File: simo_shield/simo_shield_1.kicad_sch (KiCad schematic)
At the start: 10 parts, among them J1 modulo_usb_debug, J2 conector_bateria, U1 elemon_board, U2 modulo_flash_externa, U3 bluepill_board_stm32, U4 modulo_acelerometro

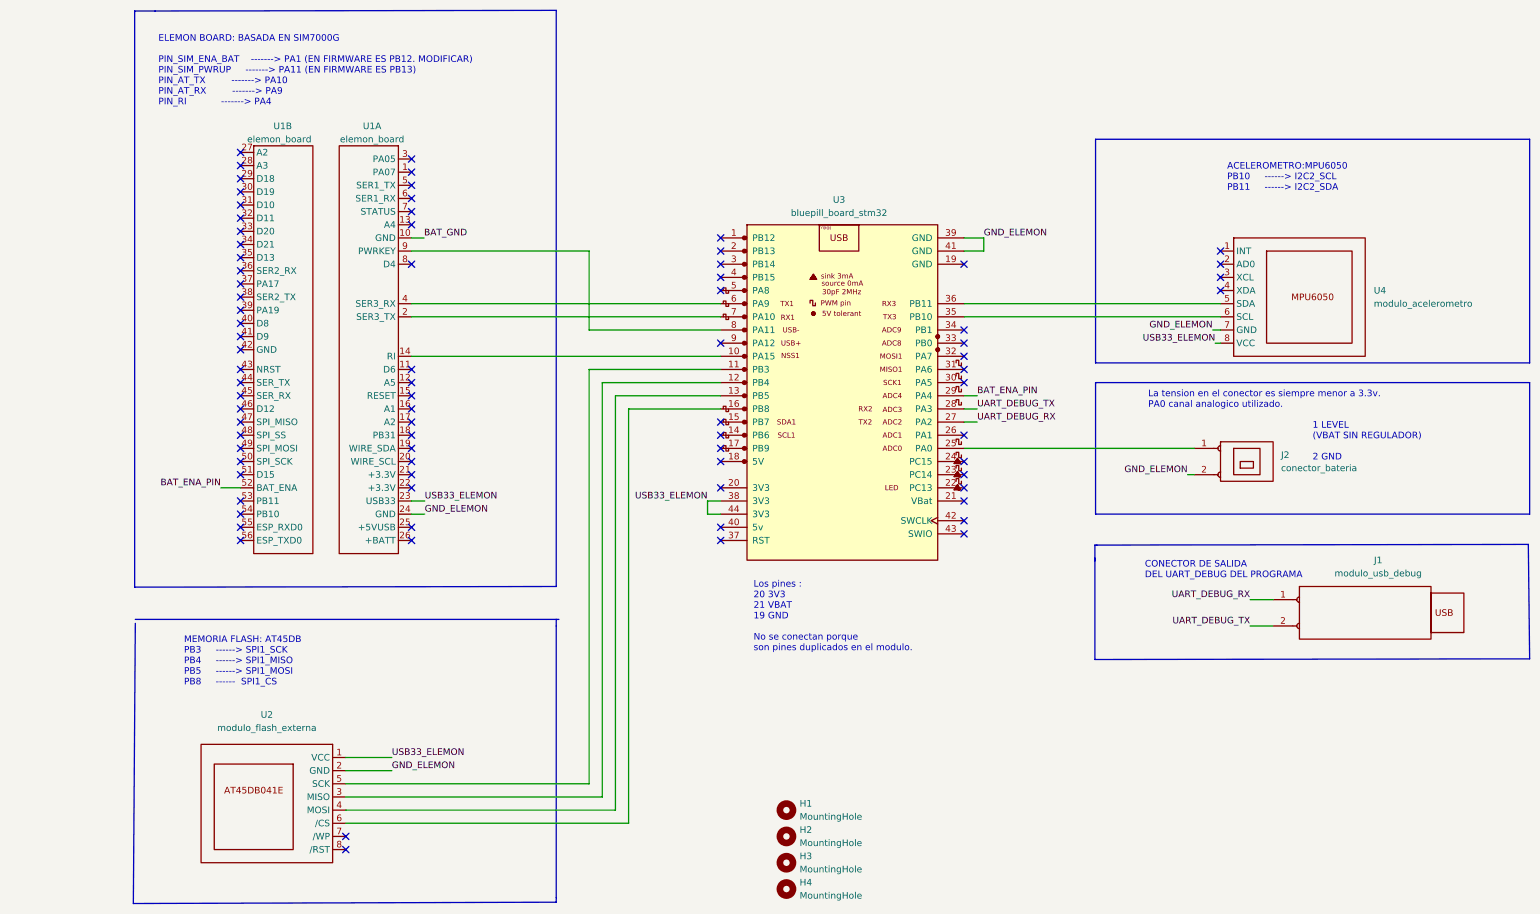
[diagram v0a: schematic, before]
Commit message: modificaciones simo shield: esquema y PCB. Detalle: se modifico la alimentacion y  eliminaron conectores custom
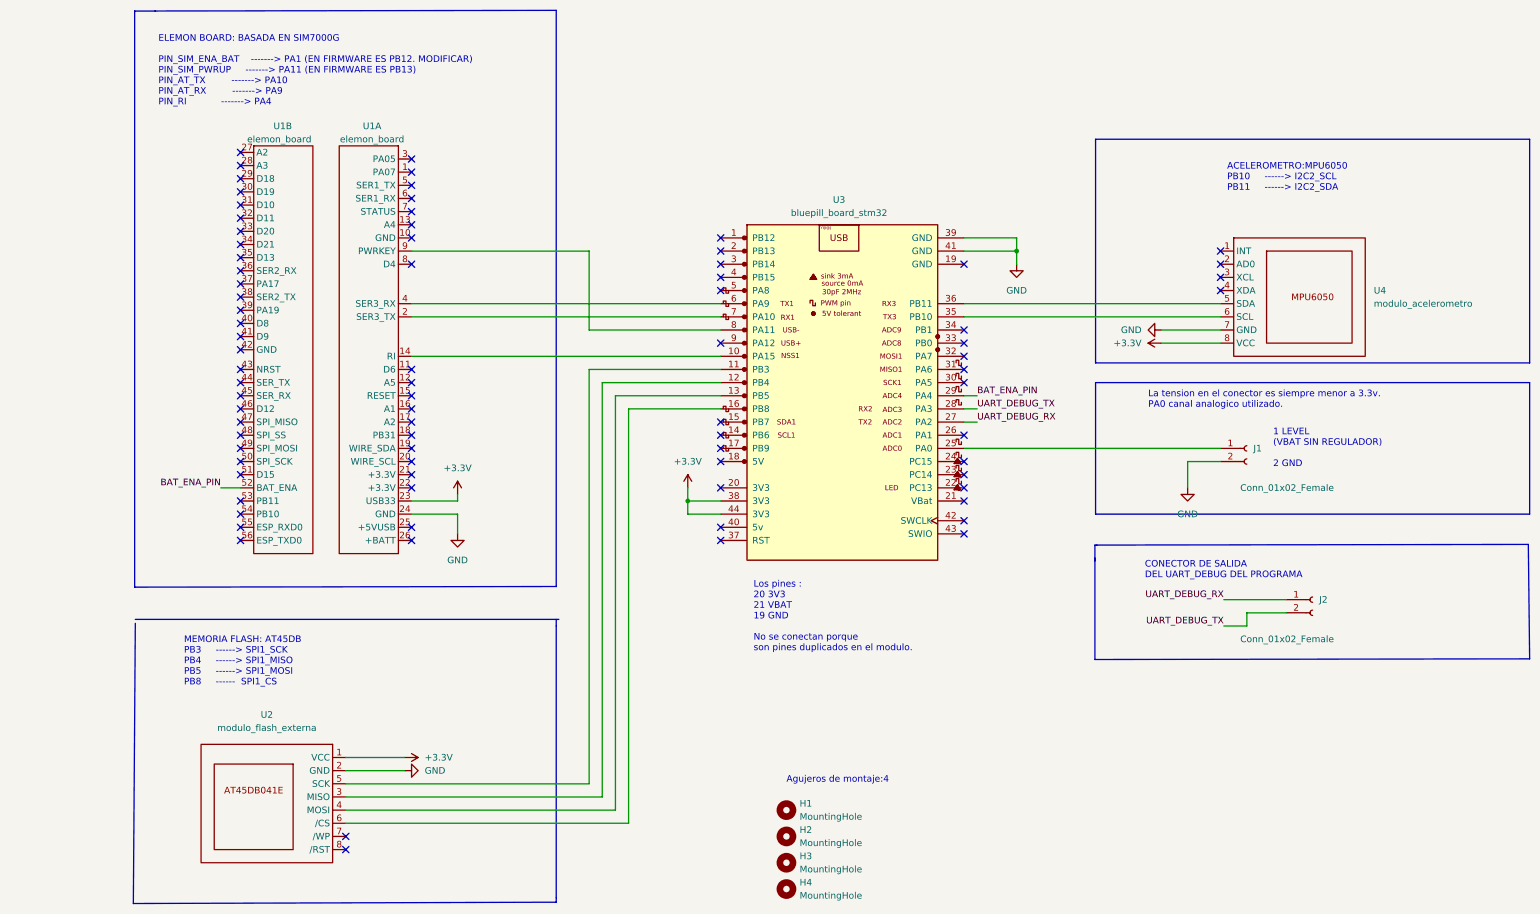
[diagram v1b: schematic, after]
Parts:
- removed J1: modulo_usb_debug, simo_shield:JST_EH_B2B-EH-A_1x02_P2.50mm_Vertical, symbol simo_shield:modulo_usb_debug
- removed J2: conector_bateria, simo_shield:JST_EH_B2B-EH-A_1x02_P2.50mm_Vertical, symbol simo_shield:conector_bateria
- added J1, J2: Conn_01x02_Female, simo_shield:JST_EH_B2B-EH-A_1x02_P2.50mm_Vertical, symbol simo_shield:Conn_01x02_Female
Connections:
- net UART_DEBUG_RX: now also J2.1 (Pin_1)
- net UART_DEBUG_TX: now also J2.2 (Pin_2)
- net at U3.25 (PA0): now also J1.1 (Pin_1)
- net BAT_GND: no longer names the net of U1.10 (GND)
- net GND_ELEMON renamed GND
- net GND: now also J1.2 (Pin_2)
- net USB33_ELEMON renamed +3.3V
- no-connect marks 80 -> 81
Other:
- note added: "Agujeros de montaje:4"

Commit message: actualizaciones a pcb y esquema simo shield
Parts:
- J1, J2: Codigo (none) -> B2B-EH-A(LF)(SN); Digikey (none) -> 455-1611-ND
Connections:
- net +3.3V: now also U4.7 (GND); no longer U4.8 (VCC)
- net GND: now also U4.8 (VCC); no longer U4.7 (GND)
- net at U1.9 (PWRKEY): now also U3.2 (PB13); no longer U3.8 (PA11)
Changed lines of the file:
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@@
   )
   (no_connect (at 127 118.11))
-  (no_connect (at 127 62.23))
+  (no_connect (at 127 77.47))
   (no_connect (at 127 69.85))
   (no_connect (at 127 80.01))
@@
     (stroke (width 0) (type default) (color 0 0 0 0))
   )
+  (wire (pts (xy 67.31 62.23) (xy 127 62.23))
+    (stroke (width 0) (type default) (color 0 0 0 0))
+  )
   (wire (pts (xy 212.09 80.01) (xy 223.52 80.01))
     (stroke (width 0) (type default) (color 0 0 0 0))
@@
     (stroke (width 0) (type default) (color 0 0 0 0))
   )
-  (wire (pts (xy 127 77.47) (xy 101.6 77.47))
-    (stroke (width 0) (type default) (color 0 0 0 0))
-  )
   (wire (pts (xy 120.65 110.49) (xy 127 110.49))
     (stroke (width 0) (type default) (color 0 0 0 0))
@@
     (stroke (width 0) (type default) (color 0 0 0 0))
   )
-  (wire (pts (xy 101.6 77.47) (xy 101.6 62.23))
-    (stroke (width 0) (type default) (color 0 0 0 0))
-  )
   (wire (pts (xy 106.68 90.17) (xy 127 90.17))
     (stroke (width 0) (type default) (color 0 0 0 0))
@@
   )
   (wire (pts (xy 224.155 134.62) (xy 228.6 134.62))
-    (stroke (width 0) (type default) (color 0 0 0 0))
-  )
-  (wire (pts (xy 67.31 62.23) (xy 101.6 62.23))
     (stroke (width 0) (type default) (color 0 0 0 0))
   )
@@
       (effects (font (size 1.27 1.27)) hide)
     )
-    (property "Datasheet" "~" (id 3) (at 228.6 100.33 0)
+    (property "Datasheet" "https://www.jst.fr/doc/jst/pdf/jst-connector-catalogue-vol-120e.pdf" (id 3) (at 228.6 100.33 0)
+      (effects (font (size 1.27 1.27)) hide)
+    )
+    (property "Digikey" "455-1611-ND" (id 4) (at 228.6 100.33 0)
+      (effects (font (size 1.27 1.27)) hide)
+    )
+    (property "Codigo" "B2B-EH-A(LF)(SN)" (id 5) (at 228.6 100.33 0)
       (effects (font (size 1.27 1.27)) hide)
     )
@@
       (effects (font (size 1.27 1.27)) hide)
     )
-    (property "Datasheet" "~" (id 3) (at 241.3 129.54 0)
+    (property "Datasheet" "https://www.jst.fr/doc/jst/pdf/jst-connector-catalogue-vol-120e.pdf" (id 3) (at 241.3 129.54 0)
+      (effects (font (size 1.27 1.27)) hide)
+    )
+    (property "Codigo" "B2B-EH-A(LF)(SN)" (id 4) (at 241.3 129.54 0)
+      (effects (font (size 1.27 1.27)) hide)
+    )
+    (property "Digikey" "455-1611-ND" (id 5) (at 241.3 129.54 0)
       (effects (font (size 1.27 1.27)) hide)
     )
@@
     (pin "2")
   )
-  (symbol (lib_id "simo_shield:+3.3V") (at 212.09 80.01 90) (unit 1)
-    (in_bom yes) (on_board yes) (fields_autoplaced)
-    (property "Reference" "#PWR0109" (id 0) (at 215.9 80.01 0)
-      (effects (font (size 1.27 1.27)) hide)
-    )
-    (property "Value" "+3.3V" (id 1) (at 208.28 80.0099 90)
-      (effects (font (size 1.27 1.27)) (justify left))
-    )
-    (property "Footprint" "" (id 2) (at 212.09 80.01 0)
-      (effects (font (size 1.27 1.27)) hide)
-    )
-    (property "Datasheet" "" (id 3) (at 212.09 80.01 0)
+  (symbol (lib_id "simo_shield:+3.3V") (at 212.09 77.47 90) (unit 1)
+    (in_bom yes) (on_board yes) (fields_autoplaced)
+    (property "Reference" "#PWR0109" (id 0) (at 215.9 77.47 0)
+      (effects (font (size 1.27 1.27)) hide)
+    )
+    (property "Value" "+3.3V" (id 1) (at 208.28 77.4699 90)
+      (effects (font (size 1.27 1.27)) (justify left))
+    )
+    (property "Footprint" "" (id 2) (at 212.09 77.47 0)
+      (effects (font (size 1.27 1.27)) hide)
+    )
+    (property "Datasheet" "" (id 3) (at 212.09 77.47 0)
       (effects (font (size 1.27 1.27)) hide)
     )
@@
     (pin "1")
   )
-  (symbol (lib_id "power:GND") (at 212.09 77.47 270) (unit 1)
-    (in_bom yes) (on_board yes) (fields_autoplaced)
-    (property "Reference" "#PWR0110" (id 0) (at 205.74 77.47 0)
-      (effects (font (size 1.27 1.27)) hide)
-    )
-    (property "Value" "GND" (id 1) (at 208.28 77.4699 90)
+  (symbol (lib_id "power:GND") (at 212.09 80.01 270) (unit 1)
+    (in_bom yes) (on_board yes) (fields_autoplaced)
+    (property "Reference" "#PWR0110" (id 0) (at 205.74 80.01 0)
+      (effects (font (size 1.27 1.27)) hide)
+    )
+    (property "Value" "GND" (id 1) (at 208.28 80.0099 90)
       (effects (font (size 1.27 1.27)) (justify right))
     )
-    (property "Footprint" "" (id 2) (at 212.09 77.47 0)
-      (effects (font (size 1.27 1.27)) hide)
-    )
-    (property "Datasheet" "" (id 3) (at 212.09 77.47 0)
-      (effects (font (size 1.27 1.27)) hide)
-    )
+    (property "Footprint" "" (id 2) (at 212.09 80.01 0)
+      (effects (font (size 1.27 1.27)) hide)
+    )
+    (property "Datasheet" "" (id 3) (at 212.09 80.01 0)
+      (effects (font (size 1.27 1.27)) hide)
+    )

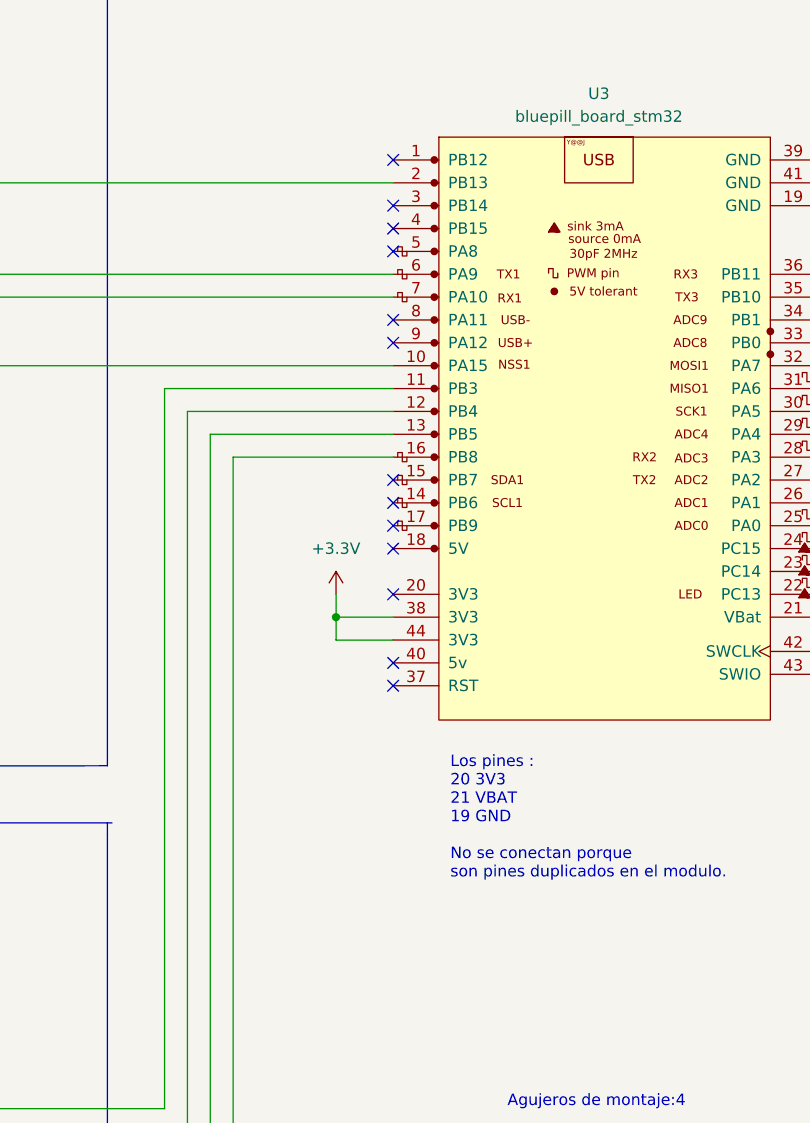
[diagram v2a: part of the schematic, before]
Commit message: update: PINB13 paso a ser PA12. Modificar en firmware
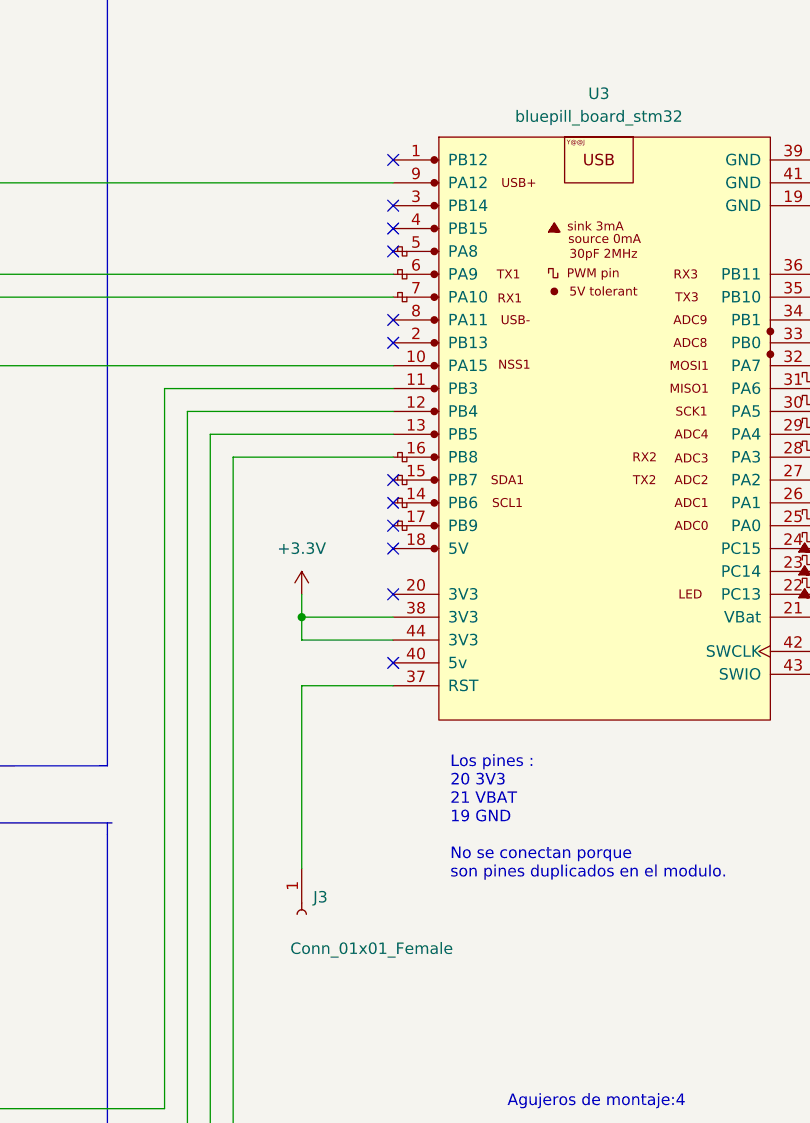
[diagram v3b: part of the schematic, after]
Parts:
- added J3: Conn_01x01_Female, Connector_PinHeader_2.54mm:PinHeader_1x01_P2.54mm_Vertical, symbol simo_shield:Conn_01x01_Female
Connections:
- net at U1.9 (PWRKEY): now also U3.9 (PA12); no longer U3.2 (PB13)
- net at U3.37 (RST): now also J3.1 (Pin_1)
- no-connect marks 81 -> 80
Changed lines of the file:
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@@
     (comment 5 "Descripcion:")
   )
-  (junction (at 120.65 110.49) (diameter 0) (color 0 0 0 0)
+  (junction (at 116.84 110.49) (diameter 0) (color 0 0 0 0)
   )
   (junction (at 184.15 62.23) (diameter 0) (color 0 0 0 0)
   )
-  (no_connect (at 127 118.11))
   (no_connect (at 127 77.47))
   (no_connect (at 127 69.85))
@@
     (stroke (width 0) (type default) (color 0 0 0 0))
   )
+  (wire (pts (xy 116.84 110.49) (xy 116.84 113.03))
+    (stroke (width 0) (type default) (color 0 0 0 0))
+  )
+  (wire (pts (xy 127 118.11) (xy 116.84 118.11))
+    (stroke (width 0) (type default) (color 0 0 0 0))
+  )
   (wire (pts (xy 173.99 92.71) (xy 176.53 92.71))
     (stroke (width 0) (type default) (color 0 0 0 0))
@@
     (stroke (width 0) (type default) (color 0 0 0 0))
   )
-  (wire (pts (xy 120.65 110.49) (xy 127 110.49))
+  (wire (pts (xy 116.84 110.49) (xy 127 110.49))
     (stroke (width 0) (type default) (color 0 0 0 0))
   )
@@
     (stroke (width 0) (type default) (color 0 0 0 0))
   )
-  (wire (pts (xy 120.65 110.49) (xy 120.65 113.03))
-    (stroke (width 0) (type default) (color 0 0 0 0))
-  )
   (wire (pts (xy 104.14 87.63) (xy 127 87.63))
     (stroke (width 0) (type default) (color 0 0 0 0))
   )
-  (wire (pts (xy 120.65 107.95) (xy 120.65 110.49))
+  (wire (pts (xy 116.84 107.95) (xy 116.84 110.49))
+    (stroke (width 0) (type default) (color 0 0 0 0))
+  )
+  (wire (pts (xy 116.84 118.11) (xy 116.84 138.43))
     (stroke (width 0) (type default) (color 0 0 0 0))
   )
@@
     (stroke (width 0) (type default) (color 0 0 0 0))
   )
-  (wire (pts (xy 120.65 113.03) (xy 127 113.03))
+  (wire (pts (xy 116.84 113.03) (xy 127 113.03))
     (stroke (width 0) (type default) (color 0 0 0 0))
   )
@@
     (pin "7")
     (pin "8")
+  )
+  (symbol (lib_id "simo_shield:Conn_01x01_Female") (at 116.84 143.51 270) (unit 1)
+    (in_bom yes) (on_board yes)
+    (property "Reference" "J3" (id 0) (at 118.11 141.6049 90)
+      (effects (font (size 1.27 1.27)) (justify left))
+    )
+    (property "Value" "Conn_01x01_Female" (id 1) (at 115.57 147.32 90)
+      (effects (font (size 1.27 1.27)) (justify left))
+    )
+    (property "Footprint" "Connector_PinHeader_2.54mm:PinHeader_1x01_P2.54mm_Vertical" (id 2) (at 116.84 143.51 0)
+      (effects (font (size 1.27 1.27)) hide)
+    )
+    (property "Datasheet" "~" (id 3) (at 116.84 143.51 0)
+      (effects (font (size 1.27 1.27)) hide)
+    )
+    (pin "1")
   )
   (symbol (lib_id "simo_shield:elemon_board") (at 64.77 40.64 0) (mirror y) (unit 1)
@@
     (pin "56")
   )
-  (symbol (lib_id "power:+3.3V") (at 120.65 107.95 0) (unit 1)
-    (in_bom yes) (on_board yes) (fields_autoplaced)
-    (property "Reference" "#PWR0102" (id 0) (at 120.65 111.76 0)
-      (effects (font (size 1.27 1.27)) hide)
-    )
-    (property "Value" "+3.3V" (id 1) (at 120.65 102.87 0))
-    (property "Footprint" "" (id 2) (at 120.65 107.95 0)
-      (effects (font (size 1.27 1.27)) hide)
-    )
-    (property "Datasheet" "" (id 3) (at 120.65 107.95 0)
+  (symbol (lib_id "power:+3.3V") (at 116.84 107.95 0) (unit 1)
+    (in_bom yes) (on_board yes) (fields_autoplaced)
+    (property "Reference" "#PWR0102" (id 0) (at 116.84 111.76 0)
+      (effects (font (size 1.27 1.27)) hide)
+    )
+    (property "Value" "+3.3V" (id 1) (at 116.84 102.87 0))
+    (property "Footprint" "" (id 2) (at 116.84 107.95 0)
+      (effects (font (size 1.27 1.27)) hide)
+    )
+    (property "Datasheet" "" (id 3) (at 116.84 107.95 0)
       (effects (font (size 1.27 1.27)) hide)
     )
@@
       (reference "J2") (unit 1) (value "Conn_01x02_Female") (footprint "simo_shield:JST_EH_B2B-EH-A_1x02_P2.50mm_Vertical")
     )
+    (path "/59284322-711a-4de1-98eb-cc82830fd394"
+      (reference "J3") (unit 1) (value "Conn_01x01_Female") (footprint "Connector_PinHeader_2.54mm:PinHeader_1x01_P2.54mm_Vertical")
+    )
     (path "/5da0ae67-8451-47ba-8f38-5b0fec97941b"

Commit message: update pcb
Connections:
- net +3.3V: now also U4.8 (VCC); no longer U4.7 (GND)
- net GND: now also U4.7 (GND); no longer U4.8 (VCC)
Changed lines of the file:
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@@
+    (stroke (width 0) (type default) (color 0 0 0 0))
+  )
+  (wire (pts (xy 212.09 77.47) (xy 223.52 77.47))
+    (stroke (width 0) (type default) (color 0 0 0 0))
+  )
+  (polyline (pts (xy 283.21 113.03) (xy 199.39 113.03))
     (stroke (width 0) (type default) (color 0 0 0 0))
   )
   (wire (pts (xy 212.09 80.01) (xy 223.52 80.01))
-    (stroke (width 0) (type default) (color 0 0 0 0))
-  )
-  (polyline (pts (xy 283.21 113.03) (xy 199.39 113.03))
-    (stroke (width 0) (type default) (color 0 0 0 0))
-  )
-  (wire (pts (xy 212.09 77.47) (xy 223.52 77.47))
     (stroke (width 0) (type default) (color 0 0 0 0))
   )
@@
     (pin "2")
   )
-  (symbol (lib_id "simo_shield:+3.3V") (at 212.09 77.47 90) (unit 1)
-    (in_bom yes) (on_board yes) (fields_autoplaced)
-    (property "Reference" "#PWR0109" (id 0) (at 215.9 77.47 0)
-      (effects (font (size 1.27 1.27)) hide)
-    )
-    (property "Value" "+3.3V" (id 1) (at 208.28 77.4699 90)
-      (effects (font (size 1.27 1.27)) (justify left))
-    )
-    (property "Footprint" "" (id 2) (at 212.09 77.47 0)
-      (effects (font (size 1.27 1.27)) hide)
-    )
-    (property "Datasheet" "" (id 3) (at 212.09 77.47 0)
+  (symbol (lib_id "simo_shield:+3.3V") (at 212.09 80.01 90) (unit 1)
+    (in_bom yes) (on_board yes) (fields_autoplaced)
+    (property "Reference" "#PWR0109" (id 0) (at 215.9 80.01 0)
+      (effects (font (size 1.27 1.27)) hide)
+    )
+    (property "Value" "+3.3V" (id 1) (at 208.28 80.0099 90)
+      (effects (font (size 1.27 1.27)) (justify left))
+    )
+    (property "Footprint" "" (id 2) (at 212.09 80.01 0)
+      (effects (font (size 1.27 1.27)) hide)
+    )
+    (property "Datasheet" "" (id 3) (at 212.09 80.01 0)
       (effects (font (size 1.27 1.27)) hide)
     )
@@
     (pin "1")
   )
-  (symbol (lib_id "power:GND") (at 212.09 80.01 270) (unit 1)
-    (in_bom yes) (on_board yes) (fields_autoplaced)
-    (property "Reference" "#PWR0110" (id 0) (at 205.74 80.01 0)
-      (effects (font (size 1.27 1.27)) hide)
-    )
-    (property "Value" "GND" (id 1) (at 208.28 80.0099 90)
+  (symbol (lib_id "power:GND") (at 212.09 77.47 270) (unit 1)
+    (in_bom yes) (on_board yes) (fields_autoplaced)
+    (property "Reference" "#PWR0110" (id 0) (at 205.74 77.47 0)
+      (effects (font (size 1.27 1.27)) hide)
+    )
+    (property "Value" "GND" (id 1) (at 208.28 77.4699 90)
       (effects (font (size 1.27 1.27)) (justify right))
     )
-    (property "Footprint" "" (id 2) (at 212.09 80.01 0)
-      (effects (font (size 1.27 1.27)) hide)
-    )
-    (property "Datasheet" "" (id 3) (at 212.09 80.01 0)
-      (effects (font (size 1.27 1.27)) hide)
-    )
+    (property "Footprint" "" (id 2) (at 212.09 77.47 0)
+      (effects (font (size 1.27 1.27)) hide)
+    )
+    (property "Datasheet" "" (id 3) (at 212.09 77.47 0)
+      (effects (font (size 1.27 1.27)) hide)
+    )
